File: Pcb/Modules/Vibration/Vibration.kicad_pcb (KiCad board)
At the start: 2 copper layers, 50.8 x 20.3 mm, 11 parts, among them J1 JACK_RJ45, P1 C+, P2 C-, X1 HOLE, X2 HOLE, X3 HOLE, X4 HOLE, X5 HOLE, X6 HOLE

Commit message: Update pcbs.
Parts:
- moved J1 0.52 mm to (30.0, 35.6)
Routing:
- net GND: track 29.7 -> 28.9 mm
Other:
- board text added: "Black"
- board text added: "Red"
- board text added: "Vibration Module 2017-12-03"
- board text removed: "Vibration Module 2017-12-1"
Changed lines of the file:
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@@
     (links 8)
     (no_connects 0)
-    (area 25.324999 25.324999 76.275001 45.795001)
+    (area 22.000869 24.0968 76.275001 47.1232)
     (thickness 1.6)
-    (drawings 16)
-    (tracks 20)
+    (drawings 18)
+    (tracks 21)
     (zones 0)
     (modules 11)
@@
   )
   (setup
-    (last_trace_width 0.254)
+    (last_trace_width 0.762)
     (user_trace_width 0.508)
     (user_trace_width 0.762)
@@
   )
   (module CA6:RJ45_pcbwing (layer F.Cu)
-    (at 30.099 36.068 270)
+    (at 29.972 35.56 270)
     (fp_text reference J1 (at 7.366 -7.112 360) (layer F.SilkS)
       (effects (font (size 0.8 0.8) (thickness 0.15)))
@@
     (pad 1 thru_hole circle (at 0 0) (size 5 5) (drill 2.5) (layers *.Cu *.Mask))
   )
+  (gr_text Black (at 69.85 33.02) (layer F.SilkS)
+    (effects (font (size 1.27 1.27) (thickness 0.254)) (justify left))
+  )
+  (gr_text Red (at 69.85 38.1) (layer F.SilkS)
+    (effects (font (size 1.27 1.27) (thickness 0.254)) (justify left))
+  )
   (gr_line (start 25.4 25.4) (end 31.75 25.4) (angle 90) (layer Edge.Cuts) (width 0.15))
   (gr_line (start 25.4 31.75) (end 25.4 25.4) (angle 90) (layer Edge.Cuts) (width 0.15))
@@
   (gr_line (start 25.4 31.75) (end 25.4 39.37) (angle 90) (layer Edge.Cuts) (width 0.15))
   (gr_line (start 76.2 31.75) (end 76.2 39.37) (angle 90) (layer Edge.Cuts) (width 0.15))
-  (gr_text "Vibration Module\n2017-12-1" (at 44.45 27.94) (layer F.SilkS)
+  (gr_text "Vibration Module\n2017-12-03" (at 44.45 27.94) (layer F.SilkS)
     (effects (font (size 1.016 1.016) (thickness 0.2032)) (justify left))
   )
   (gr_line (start 69.85 45.72) (end 31.75 45.72) (angle 90) (layer Edge.Cuts) (width 0.15))
   (gr_line (start 31.75 25.4) (end 69.85 25.4) (angle 90) (layer Edge.Cuts) (width 0.15))
+  (segment (start 31.872 32) (end 38.604 32) (width 0.762) (layer F.Cu) (net 1))
+  (segment (start 41.414 34.81) (end 43.18 34.81) (width 0.762) (layer F.Cu) (net 1))
+  (segment (start 38.604 32) (end 41.414 34.81) (width 0.762) (layer F.Cu) (net 1))
   (segment (start 49.21 34.56) (end 50.53 34.56) (width 0.762) (layer F.Cu) (net 1) (status 10))
   (segment (start 52.07 33.02) (end 57.15 33.02) (width 0.762) (layer F.Cu) (net 1) (status 20))
@@
   (segment (start 45.974 33.274) (end 48.768 33.274) (width 0.762) (layer F.Cu) (net 1))
   (segment (start 44.438 34.81) (end 45.974 33.274) (width 0.762) (layer F.Cu) (net 1))
-  (segment (start 31.999 32.508) (end 40.878 32.508) (width 0.762) (layer F.Cu) (net 1) (status 10))
-  (segment (start 40.878 32.508) (end 43.18 34.81) (width 0.762) (layer F.Cu) (net 1) (status 20))
-  (segment (start 31.999 28.698) (end 31.239 27.938) (width 0.254) (layer F.Cu) (net 1) (status 30))
   (segment (start 49.21 34.56) (end 49.387 34.56) (width 0.254) (layer F.Cu) (net 1) (status 30))
+  (segment (start 43.18 36.31) (end 41.414 36.31) (width 0.762) (layer F.Cu) (net 2))
+  (segment (start 39.634 38.09) (end 31.872 38.09) (width 0.762) (layer F.Cu) (net 2))
+  (segment (start 41.414 36.31) (end 39.634 38.09) (width 0.762) (layer F.Cu) (net 2))
   (segment (start 48.26 36.56) (end 50.53 36.56) (width 0.762) (layer F.Cu) (net 2) (status 10))
   (segment (start 52.07 38.1) (end 57.15 38.1) (width 0.762) (layer F.Cu) (net 2) (status 20))
@@
   (segment (start 43.18 36.31) (end 48.01 36.31) (width 0.762) (layer F.Cu) (net 2) (status 30))
   (segment (start 48.01 36.31) (end 48.26 36.56) (width 0.762) (layer F.Cu) (net 2) (status 30))
-  (segment (start 31.999 38.598) (end 40.892 38.598) (width 0.762) (layer F.Cu) (net 2) (status 10))
-  (segment (start 40.892 38.598) (end 43.18 36.31) (width 0.762) (layer F.Cu) (net 2) (status 20))
   (segment (start 48.01 36.31) (end 48.26 36.56) (width 0.254) (layer F.Cu) (net 2) (status 30))
   (zone (net 1) (net_name GND) (layer B.Cu) (hatch edge 0.508)

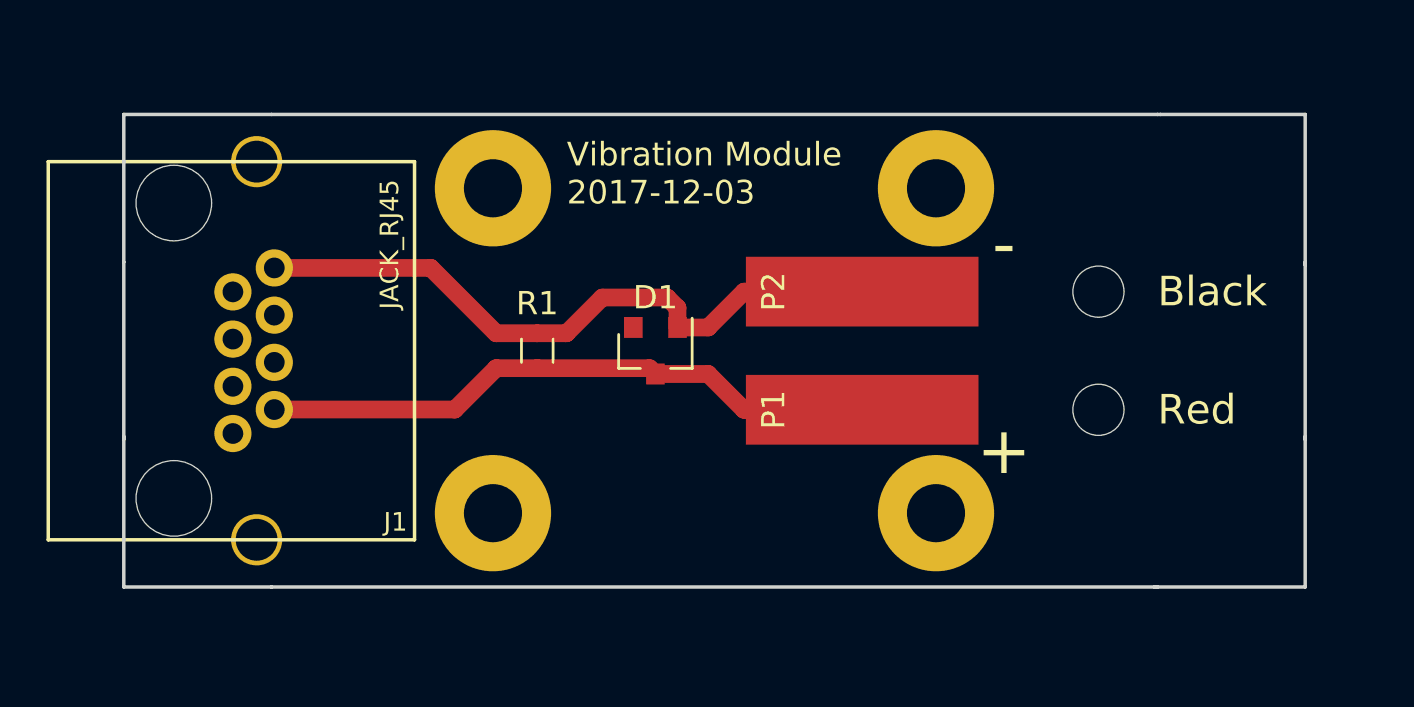
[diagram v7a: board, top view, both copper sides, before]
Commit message: Update module pcbs
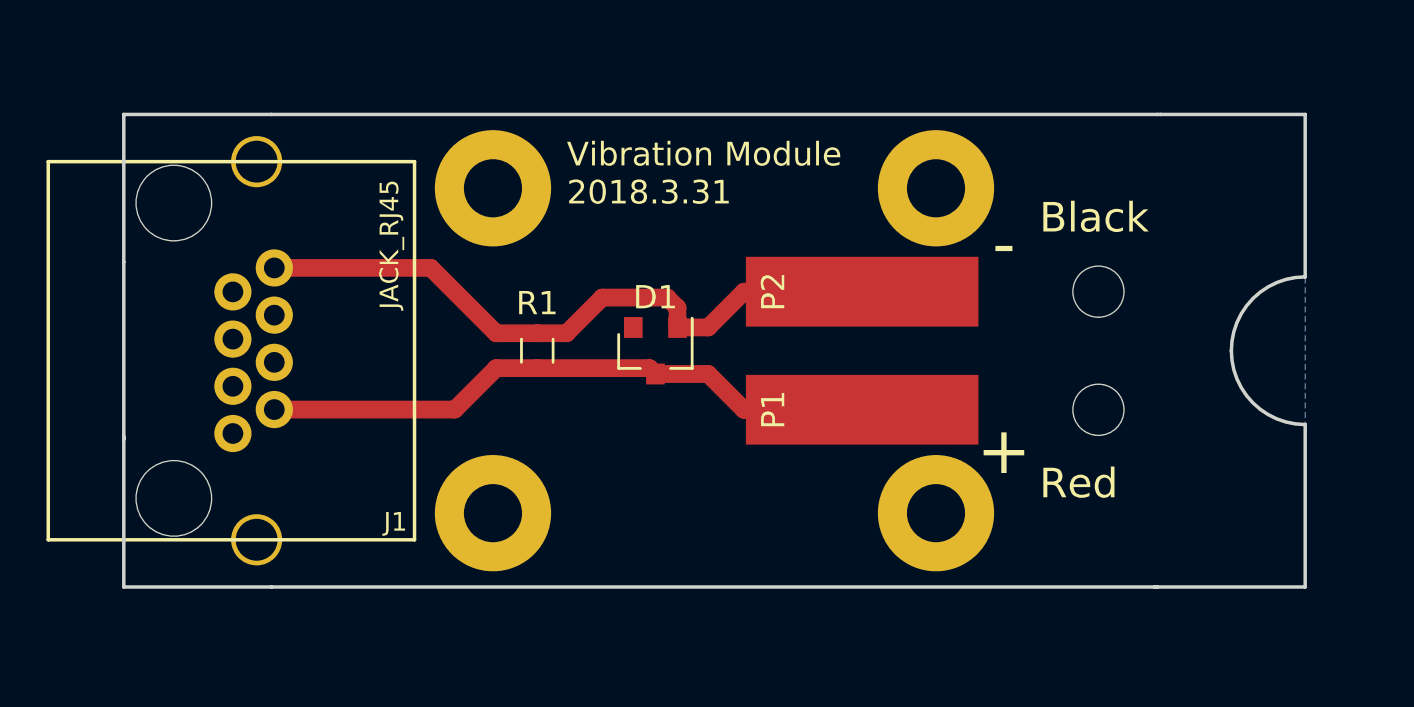
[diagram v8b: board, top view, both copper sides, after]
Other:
- outline, holes or cut-outs redrawn
- board text added: "Vibration Module 2018.3.31"
- board text removed: "Vibration Module 2017-12-03"
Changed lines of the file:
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@@
     (area 21.873869 24.0968 76.275001 47.1232)
     (thickness 1.6)
-    (drawings 18)
+    (drawings 19)
     (tracks 21)
     (zones 0)
@@
       (effects (font (size 1 1) (thickness 0.15)))
     )
-    (fp_text user %R (at 0.3 0) (layer F.Fab)
+    (fp_text user %R (at 0.3 0) (layer F.Fab) hide
       (effects (font (size 1 1) (thickness 0.15)))
     )
@@
     (pad 1 thru_hole circle (at 0 0) (size 5 5) (drill 2.5) (layers *.Cu *.Mask))
   )
-  (gr_text Black (at 69.85 33.02) (layer F.SilkS)
+  (gr_line (start 76.2 32.385) (end 76.2 25.4) (angle 90) (layer Edge.Cuts) (width 0.15))
+  (gr_line (start 76.2 45.72) (end 76.2 38.735) (angle 90) (layer Edge.Cuts) (width 0.15))
+  (gr_arc (start 76.2 35.56) (end 76.2 38.735) (angle 90) (layer Edge.Cuts) (width 0.15))
+  (gr_arc (start 76.2 35.56) (end 73.025 35.56) (angle 90) (layer Edge.Cuts) (width 0.15))
+  (gr_text Black (at 64.77 29.845) (layer F.SilkS)
     (effects (font (size 1.27 1.27) (thickness 0.254)) (justify left))
   )
-  (gr_text Red (at 69.85 38.1) (layer F.SilkS)
+  (gr_text Red (at 64.77 41.275) (layer F.SilkS)
     (effects (font (size 1.27 1.27) (thickness 0.254)) (justify left))
   )
@@
   (gr_line (start 31.75 45.72) (end 25.4 45.72) (angle 90) (layer Edge.Cuts) (width 0.15))
   (gr_line (start 69.977 25.4) (end 69.85 25.4) (angle 90) (layer Edge.Cuts) (width 0.15))
-  (gr_line (start 76.2 25.4) (end 76.2 31.877) (angle 90) (layer Edge.Cuts) (width 0.15))
   (gr_line (start 69.977 25.4) (end 76.2 25.4) (angle 90) (layer Edge.Cuts) (width 0.15))
-  (gr_line (start 76.2 45.72) (end 76.2 39.243) (angle 90) (layer Edge.Cuts) (width 0.15))
   (gr_line (start 69.723 45.72) (end 76.2 45.72) (angle 90) (layer Edge.Cuts) (width 0.15))
   (gr_text + (at 63.246 39.878) (layer F.SilkS)
@@
   )
   (gr_line (start 25.4 31.75) (end 25.4 39.37) (angle 90) (layer Edge.Cuts) (width 0.15))
-  (gr_line (start 76.2 31.75) (end 76.2 39.37) (angle 90) (layer Edge.Cuts) (width 0.15))
-  (gr_text "Vibration Module\n2017-12-03" (at 44.45 27.94) (layer F.SilkS)
+  (gr_text "Vibration Module\n2018.3.31" (at 44.45 27.94) (layer F.SilkS)
     (effects (font (size 1.016 1.016) (thickness 0.2032)) (justify left))
   )
